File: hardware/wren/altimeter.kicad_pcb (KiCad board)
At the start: 4 copper layers, 12 x 34 mm, 40 parts, among them J1 USB_C_Receptacle_USB2.0_16P, J2 Conn_01x05_MountingPin, SW2 SW_SPDT, U1 nRF52833_QDxx, U2 MCP73832T-2, U3 BMP390L, U4 W25X40CLUXIG, U5 LIS2DH, Y1 32MHz

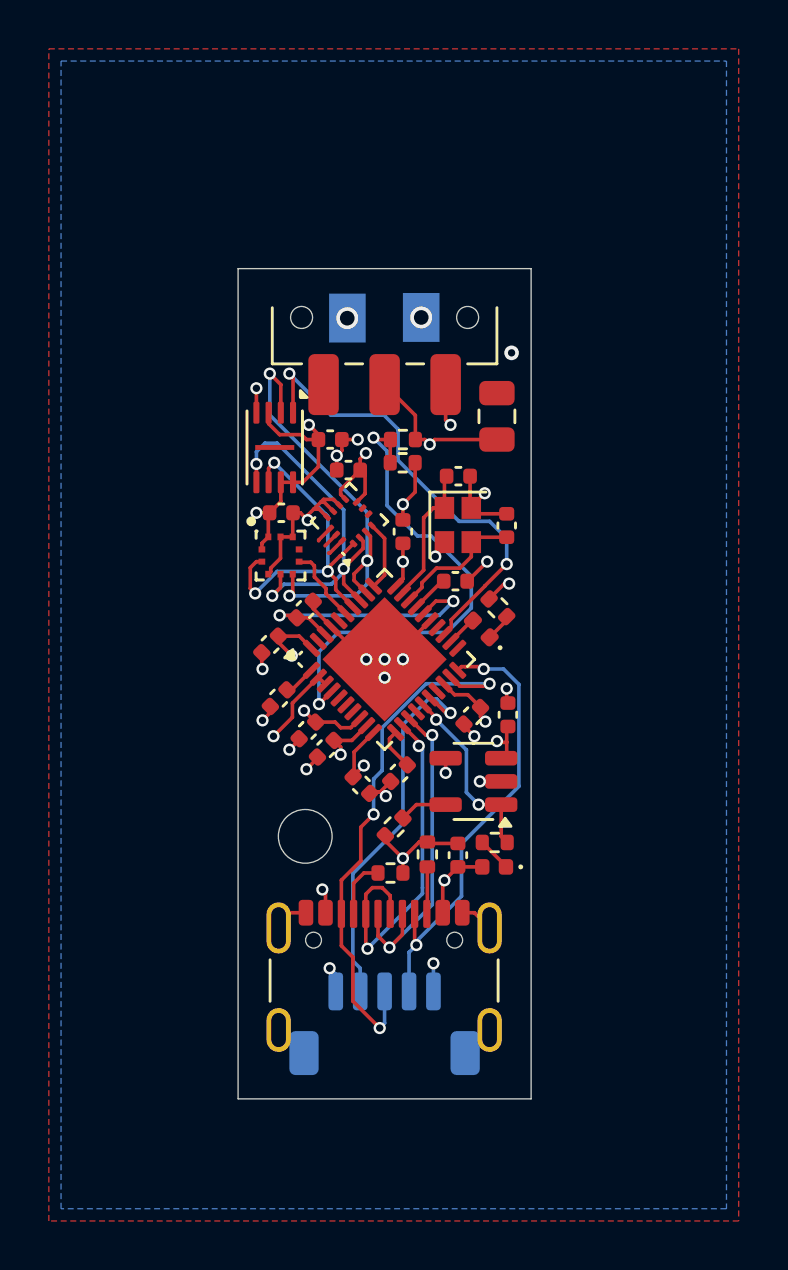
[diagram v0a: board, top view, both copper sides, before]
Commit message: Add bluetooth board
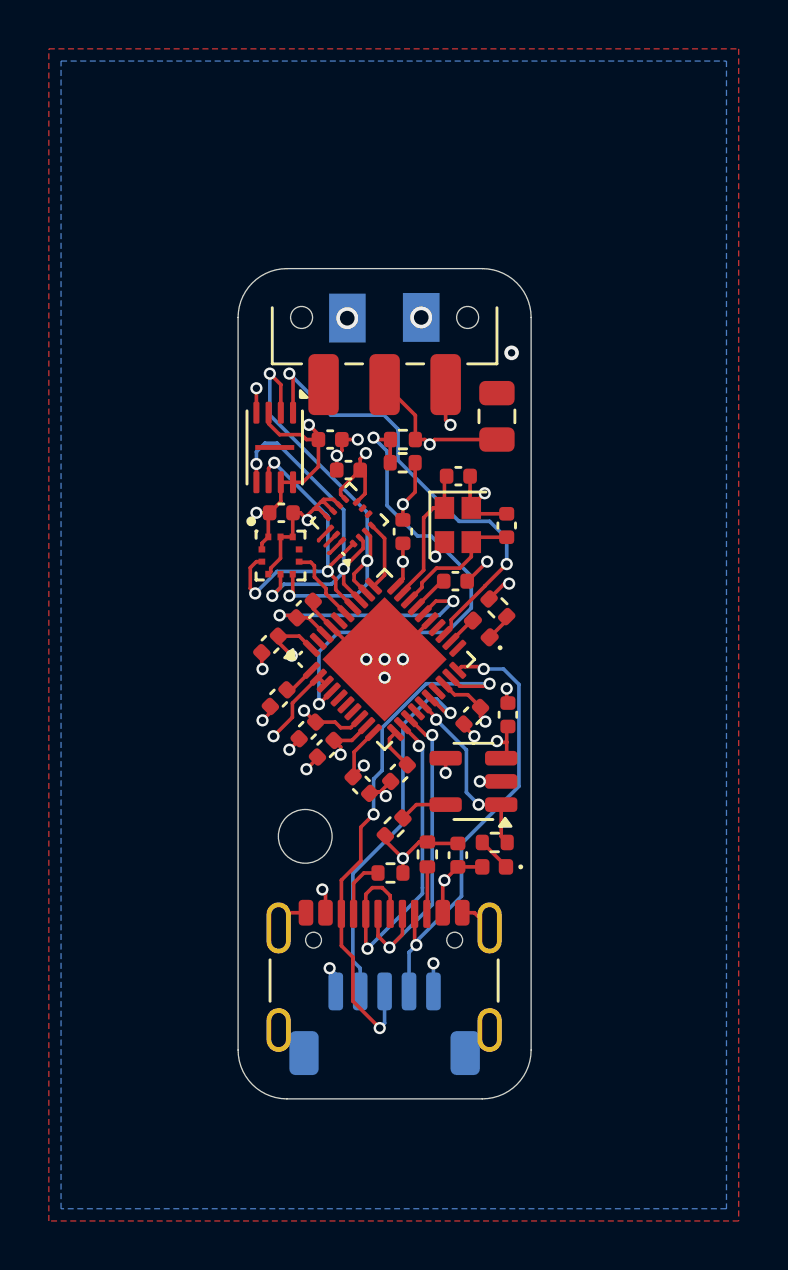
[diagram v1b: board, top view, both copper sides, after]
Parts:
- C15, C16: value 12p -> 10p
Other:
- outline, holes or cut-outs redrawn
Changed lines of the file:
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@@
 			)
 		)
-		(property "LCSC" "C779278"
+		(property "LCSC" "C2684802"
 			(at 0 0 90)
 			(unlocked yes)
@@
 			)
 		)
-		(property "LCSC" "C187794"
+		(property "LCSC" "C388796"
 			(at 0 0 -90)
 			(unlocked yes)
@@
 			)
 		)
-		(property "Value" "12p"
+		(property "Value" "10p"
 			(at 0 1.16 90)
 			(layer "F.Fab")
@@
 			)
 		)
-		(property "LCSC" ""
+		(property "LCSC" "C32949"
 			(at 0 0 90)
 			(unlocked yes)
@@
 			)
 		)
-		(property "Value" "12p"
+		(property "Value" "10p"
 			(at 0 1.16 0)
 			(layer "F.Fab")
@@
 			)
 		)
-		(property "LCSC" ""
+		(property "LCSC" "C32949"
 			(at 0 0 180)
 			(unlocked yes)
@@
 		)
 	)
-	(gr_rect
-		(start 52.5 35.75)
-		(end 64.5 69.75)
+	(gr_arc
+		(start 62.5 35.75)
+		(mid 63.914214 36.335786)
+		(end 64.5 37.75)
+		(stroke
+			(width 0.05)
+			(type default)
+		)
+		(layer "Edge.Cuts")
+	)
+	(gr_arc
+		(start 52.5 37.75)
+		(mid 53.085786 36.335786)
+		(end 54.5 35.75)
+		(stroke
+			(width 0.05)
+			(type default)
+		)
+		(layer "Edge.Cuts")
+	)
+	(gr_line
+		(start 62.5 69.75)
+		(end 54.5 69.75)
+		(stroke
+			(width 0.05)
+			(type default)
+		)
+		(layer "Edge.Cuts")
+	)
+	(gr_arc
+		(start 54.5 69.75)
+		(mid 53.085786 69.164214)
+		(end 52.5 67.75)
+		(stroke
+			(width 0.05)
+			(type default)
+		)
+		(layer "Edge.Cuts")
+	)
+	(gr_line
+		(start 52.5 67.75)
+		(end 52.5 37.75)
+		(stroke
+			(width 0.05)
+			(type default)
+		)
+		(layer "Edge.Cuts")
+	)
+	(gr_line
+		(start 64.5 37.75)
+		(end 64.5 67.75)
+		(stroke
+			(width 0.05)
+			(type default)
+		)
+		(layer "Edge.Cuts")
+	)
+	(gr_line
+		(start 54.5 35.75)
+		(end 62.5 35.75)
+		(stroke
+			(width 0.05)
+			(type default)
+		)
+		(layer "Edge.Cuts")
+	)
+	(gr_arc
+		(start 64.5 67.75)
+		(mid 63.914214 69.164214)
+		(end 62.5 69.75)
 		(stroke
 			(width 0.05)
 			(type default)
 		)
-		(fill none)
 		(layer "Edge.Cuts")
 	)
